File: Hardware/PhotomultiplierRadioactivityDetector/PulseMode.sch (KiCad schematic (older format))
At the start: 15 parts

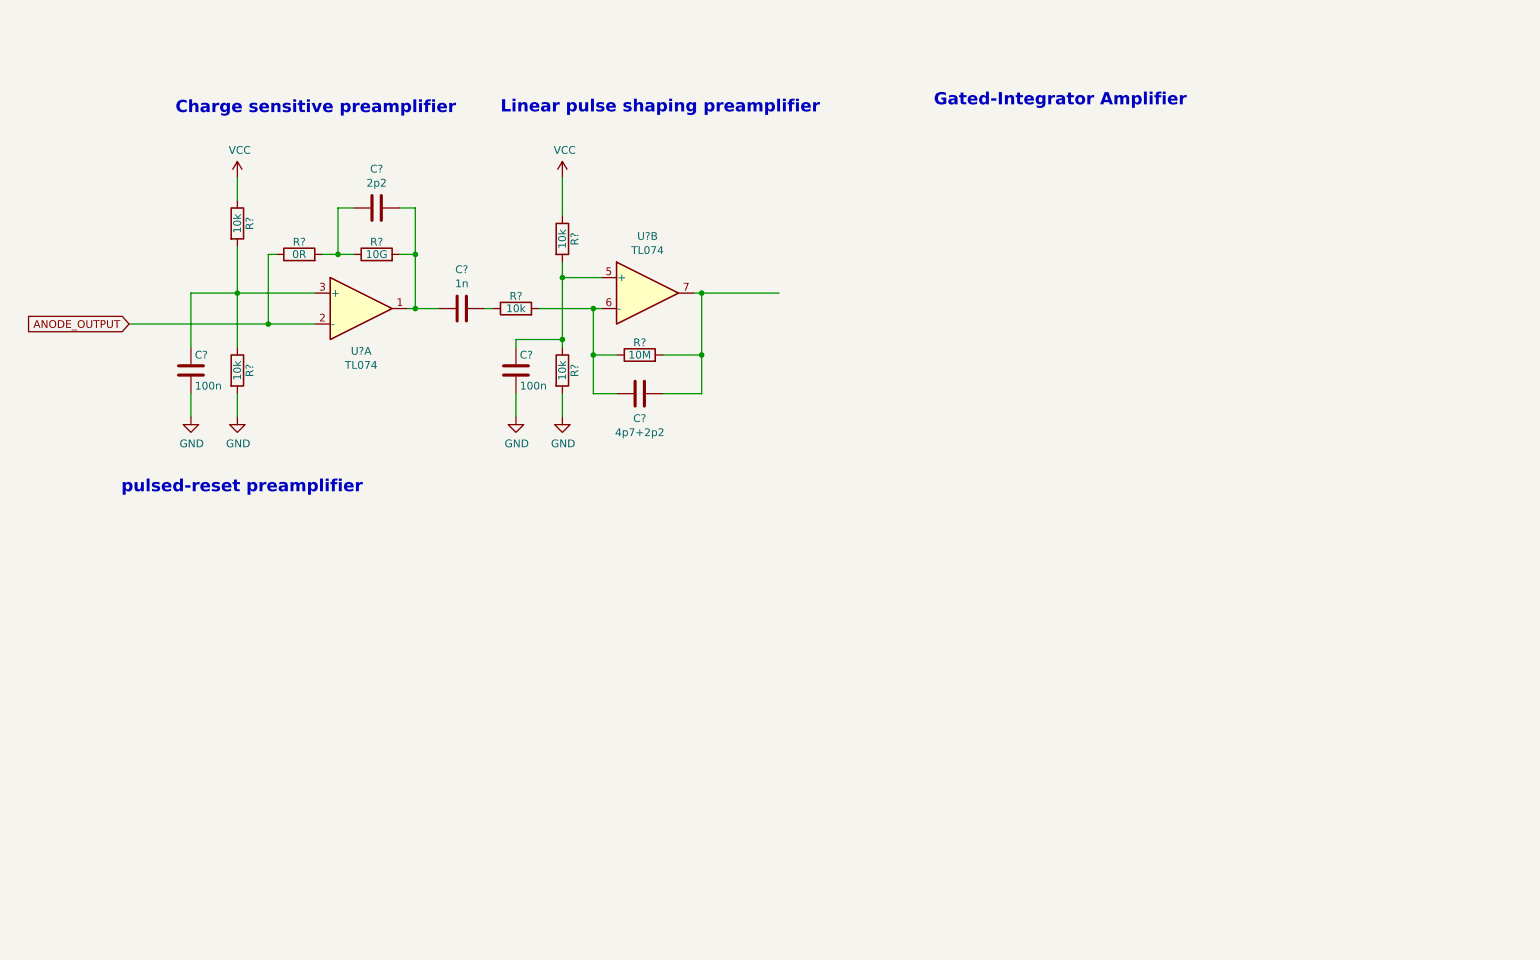
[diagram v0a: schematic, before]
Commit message: add element,, footprint and 3d model for transformer
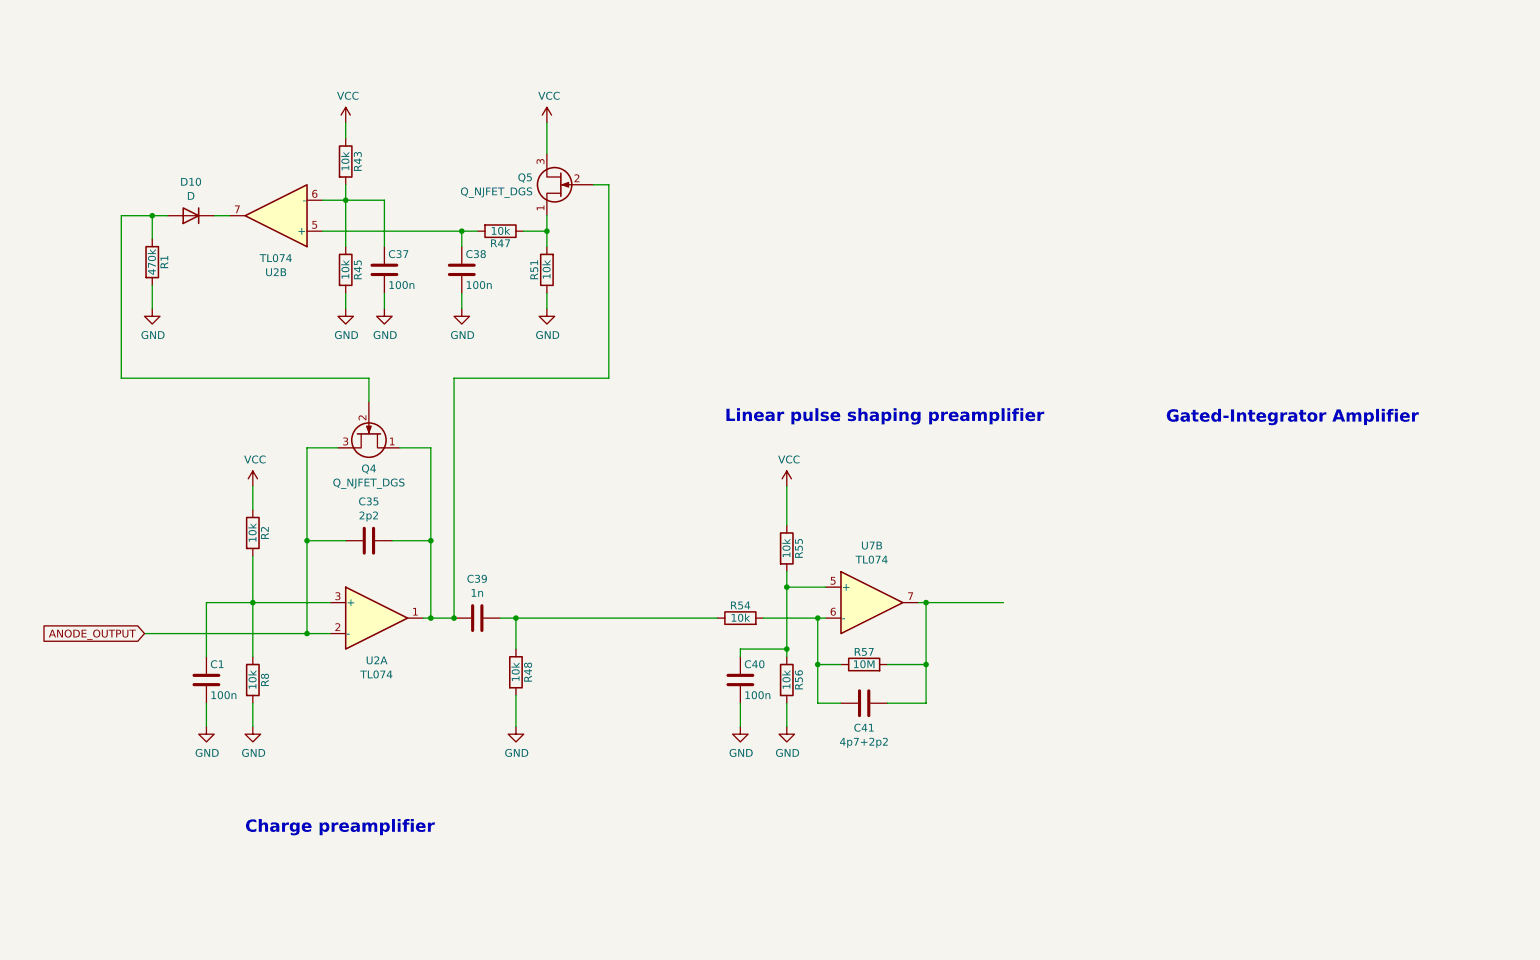
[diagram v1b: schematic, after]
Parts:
- removed R?: 10G, Resistor_SMD:R_0805_2012Metric_Pad1.15x1.40mm_HandSolder, symbol Device:R
- removed R?: 0R, Resistor_SMD:R_0805_2012Metric_Pad1.15x1.40mm_HandSolder, symbol Device:R
- added C37, C38: 100n, Capacitor_SMD:C_0805_2012Metric_Pad1.15x1.40mm_HandSolder, symbol Device:C
- added D10: D, symbol Device:D
- added Q4, Q5: Q_NJFET_DGS, Package_TO_SOT_SMD:SC-59, symbol Device:Q_NJFET_DGS
- added R1: 470k, Resistor_SMD:R_0805_2012Metric_Pad1.15x1.40mm_HandSolder, symbol Device:R
- added R43, R45, R47, R48, R51: 10k, Resistor_SMD:R_0805_2012Metric_Pad1.15x1.40mm_HandSolder, symbol Device:R
- added unit 2 of U2
- gave numbers to parts that had none: 13
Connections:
- net ANODE_OUTPUT: now also C35.2, Q4.3 (S)
- net GND: now also C37.2, C38.2, R1.2, R45.2, R48.2, R51.1
- net VCC: now also Q5.3 (S), R43.1
- net at C35.1, C39.2, U2.1: now also Q4.1 (D), Q5.2 (G)
- net at C39.1, R54.1: now also R48.1
- new net: D10.2 (A), Q4.2 (G), R1.1
- new net: C38.1, R47.2, U2.5 (+)
- new net: C37.1, R43.2, R45.1, U2.6 (-)
- new net: D10.1 (K), U2.7
- new net: Q5.1 (D), R47.1, R51.2
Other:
- note added: "Charge preamplifier\n"
- note removed: "Charge sensitive preamplifier\n"
- note removed: "pulsed-reset preamplifier\n"
- moved on the sheet: C1, C35, C39, C40, C41, R2, R54, R55, R56, R57, R8, U2A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

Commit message: fix footprints
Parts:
- D10: footprint (none) -> Diode_SMD:D_MiniMELF
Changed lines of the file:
@@
 F 0 "D10" H 2000 1783 50  0000 C CNN
 F 1 "D" H 2000 1874 50  0000 C CNN
-F 2 "" H 2000 2000 50  0001 C CNN
+F 2 "Diode_SMD:D_MiniMELF" H 2000 2000 50  0001 C CNN
 F 3 "~" H 2000 2000 50  0001 C CNN
 	1    2000 2000

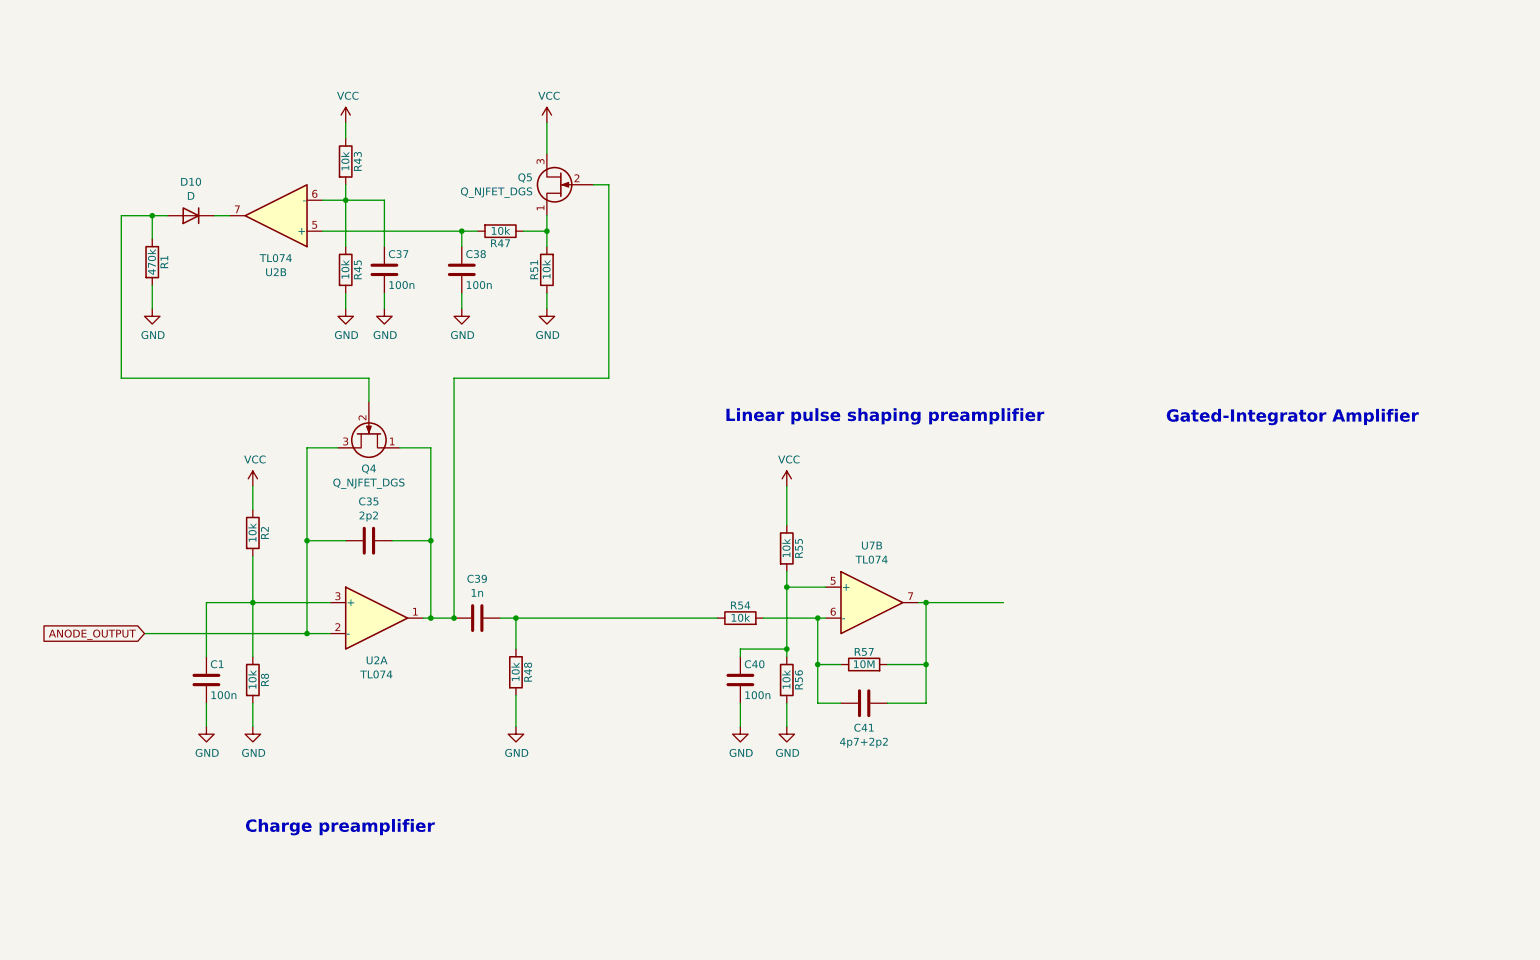
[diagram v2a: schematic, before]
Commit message: align to ltspice simulation
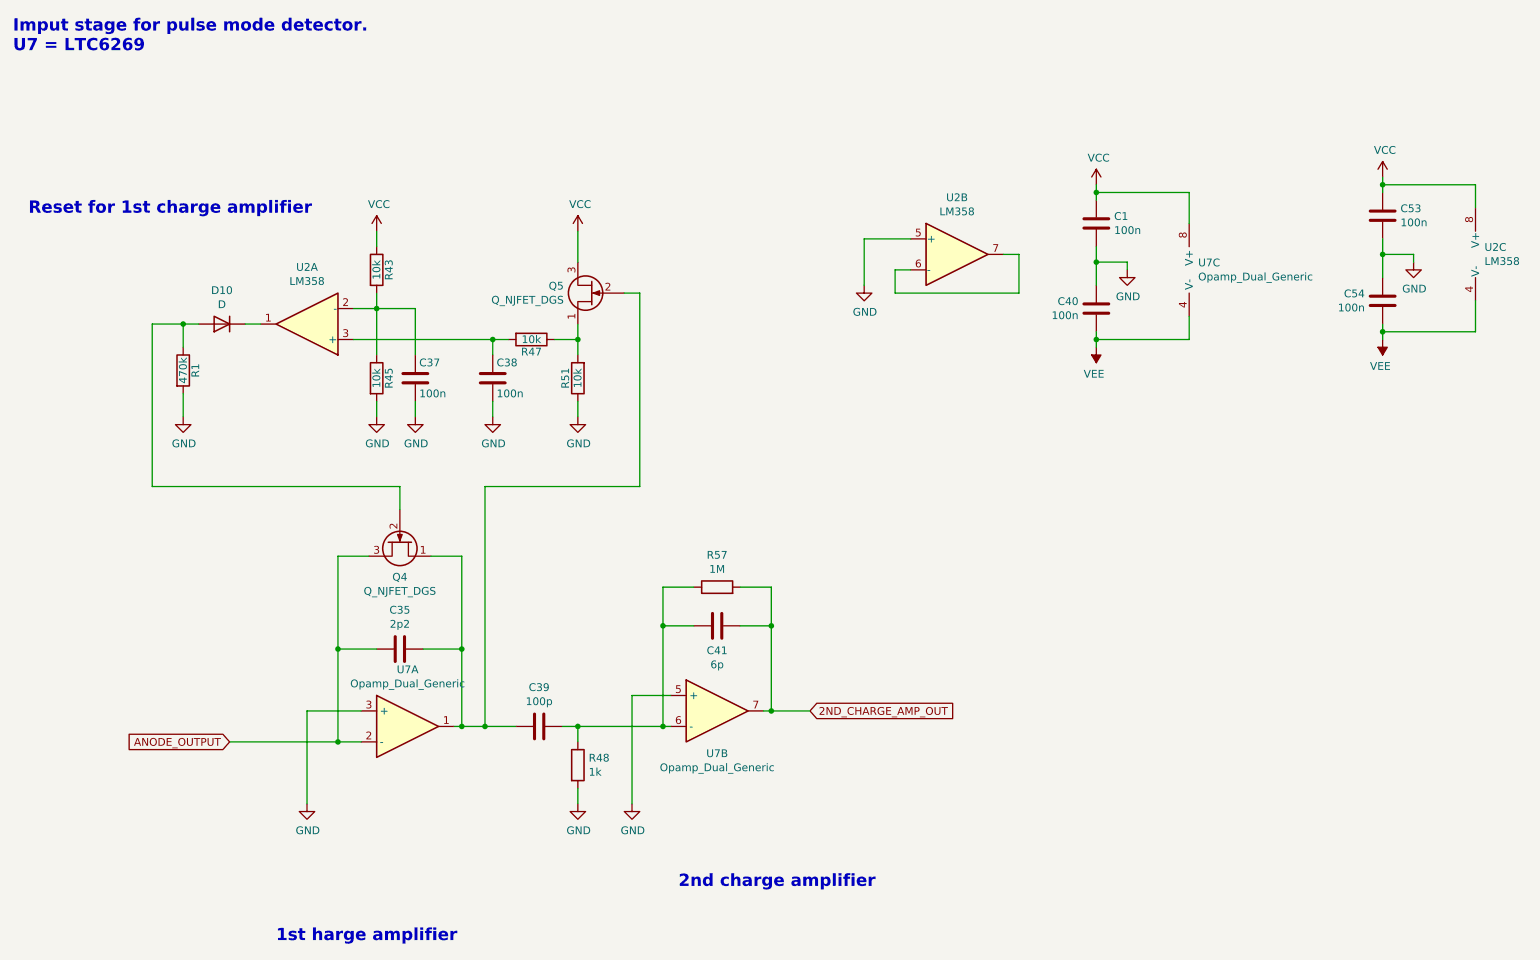
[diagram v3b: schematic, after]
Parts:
- removed R2, R54, R55, R56, R8: 10k, Resistor_SMD:R_0805_2012Metric_Pad1.15x1.40mm_HandSolder, symbol Device:R
- removed U2, U7: TL074, Package_SO:SOIC-14_3.9x8.7mm_P1.27mm, symbol Amplifier_Operational:TL074
- added C53, C54: 100n, Capacitor_SMD:C_0805_2012Metric_Pad1.15x1.40mm_HandSolder, symbol Device:C
- added U2: LM358, Package_SO:SO-8_5.3x6.2mm_P1.27mm, symbol Amplifier_Operational:LM358
- added U7: Opamp_Dual_Generic, Package_SO:MSOP-8-1EP_3x3mm_P0.65mm_EP1.68x1.88mm, symbol Device:Opamp_Dual_Generic
- C39: value 1n -> 100p
- C41: value 4p7+2p2 -> 6p
- R48: value 10k -> 1k
- R57: value 10M -> 1M
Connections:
- net ANODE_OUTPUT: now also U7.2 (-)
- net GND: now also C40.1, C53.2, C54.1, U2.5 (+), U7.3 (+), U7.5 (+); no longer C40.2
- net VCC: now also C1.1, C53.1, U2.8 (V+), U7.8 (V+)
- net at C35.1, C39.2, Q4.1 (D)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: now also U7.1
- net at C39.1, R48.1: now also C41.2, R57.1, U7.6 (-)
- net 2ND_CHARGE_AMP_OUT: now reaches C41.1, R57.2
- net 2ND_CHARGE_AMP_OUT: now also U7.7
- net at C38.1, R47.2: now also U2.3 (+)
- net at C37.1, R43.2, R45.1: now also U2.2 (-)
- net at D10.1 (K): now also U2.1
- new net: U2.6 (-), U2.7
- new net VEE: C40.2, C54.2, U2.4 (V-), U7.4 (V-)
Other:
- note added: "1st harge amplifier"
- note added: "2nd charge amplifier"
- note added: "Imput stage for pulse mode detector.\nU7 = LTC6269"
- note added: "Reset for 1st charge amplifier"
- note removed: "Charge preamplifier\n"
- note removed: "Gated-Integrator Amplifier"
- note removed: "Linear pulse shaping preamplifier\n\n\n"
- moved on the sheet: C35, C37, C38, C39, C41, D10, Q4, Q5, R1, R43, R45, R47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
